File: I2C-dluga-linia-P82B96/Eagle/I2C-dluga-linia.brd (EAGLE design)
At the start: 100 x 80 mm, 7 parts

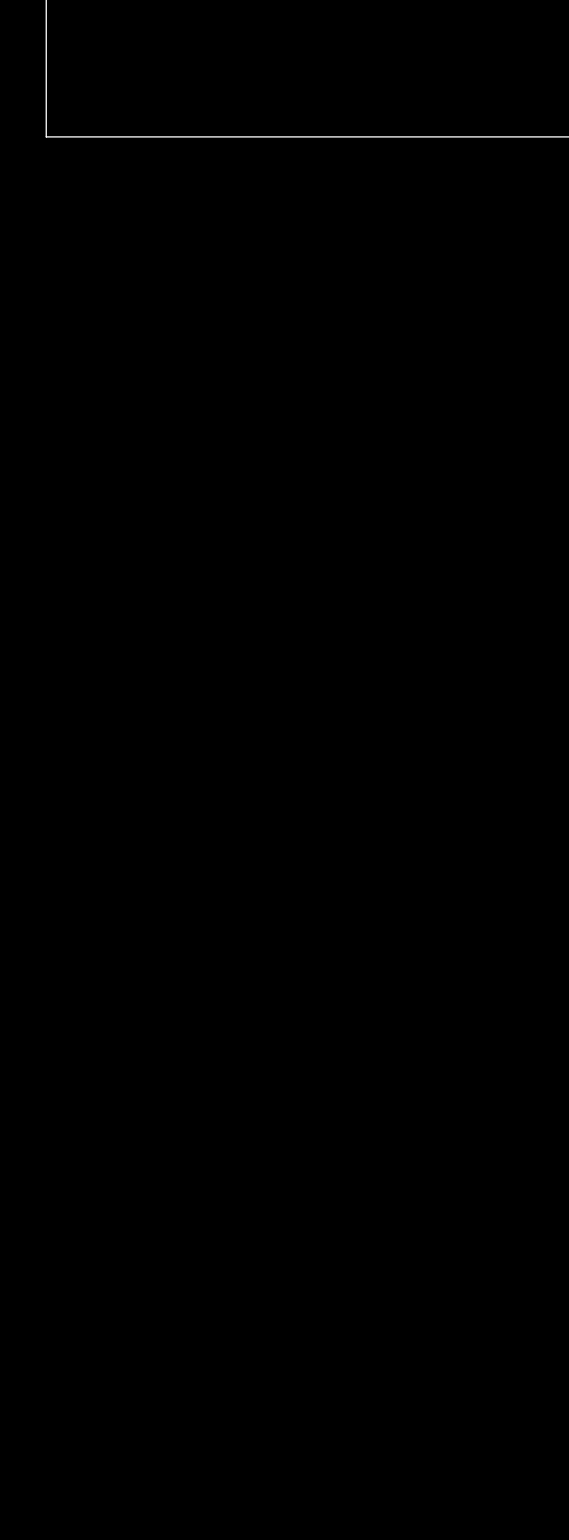
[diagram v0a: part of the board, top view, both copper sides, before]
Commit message: złącza do układów
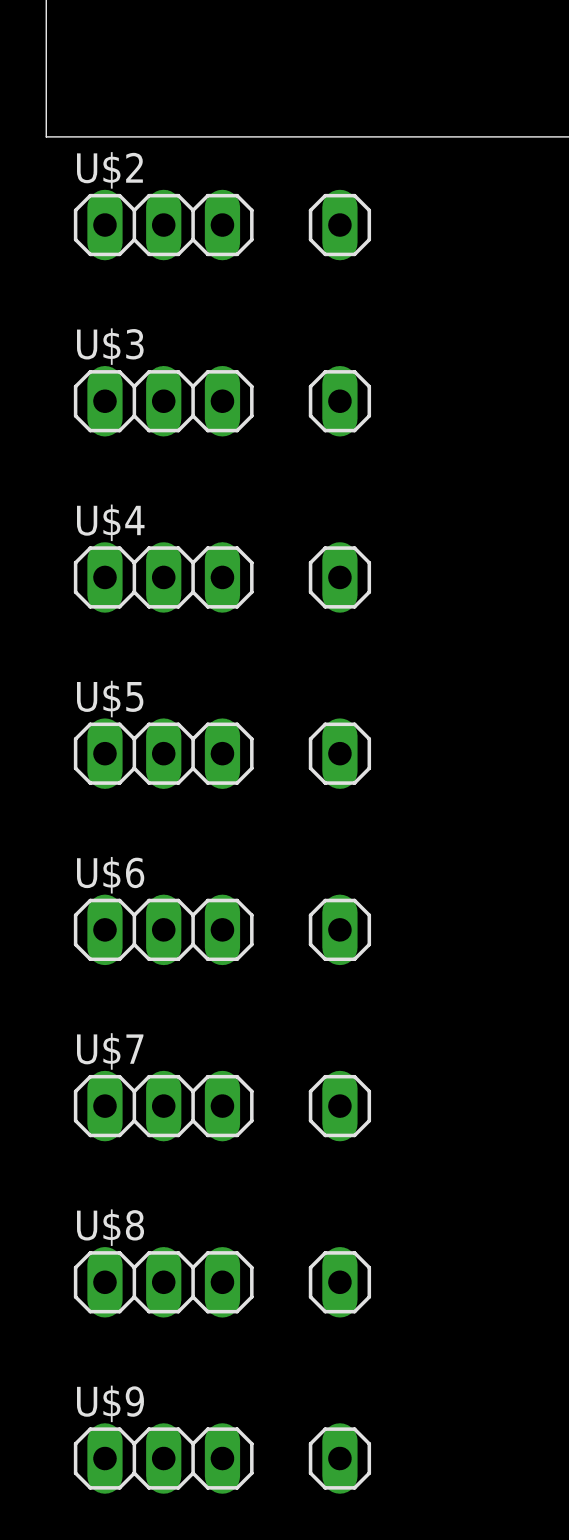
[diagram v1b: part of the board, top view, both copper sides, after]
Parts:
- added U$2, U$3, U$4, U$5, U$6, U$7, U$8, U$9: PINHD5-4, RD:1X5-4
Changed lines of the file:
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@@
 <?xml version="1.0" encoding="utf-8"?>
 <!DOCTYPE eagle SYSTEM "eagle.dtd">
-<eagle version="7.3.0">
+<eagle version="6.4">
 <drawing>
 <settings>
@@
 <pass name="Default">
 <param name="RoutingGrid" value="50mil"/>
-<param name="AutoGrid" value="1"/>
-<param name="Efforts" value="0"/>
-<param name="TopRouterVariant" value="1"/>
 <param name="tpViaShape" value="round"/>
-<param name="PrefDir.1" value="a"/>
+<param name="PrefDir.1" value="|"/>
 <param name="PrefDir.2" value="0"/>
 <param name="PrefDir.3" value="0"/>
@@
 <param name="PrefDir.14" value="0"/>
 <param name="PrefDir.15" value="0"/>
-<param name="PrefDir.16" value="a"/>
+<param name="PrefDir.16" value="-"/>
 <param name="cfVia" value="8"/>
 <param name="cfNonPref" value="5"/>
@@
 <element name="R4" library="resistor" package="R1206" value="2.2k" x="34.29" y="46.99" rot="R90"/>
 <element name="U$1" library="P82B96" package="SOIC8" value="P82B96" x="27.94" y="46.355" rot="R270"/>
+<element name="U$2" library="RD" package="1X5-4" value="PINHD5-4" x="7.62" y="-3.81"/>
+<element name="U$3" library="RD" package="1X5-4" value="PINHD5-4" x="7.62" y="-11.43"/>
+<element name="U$4" library="RD" package="1X5-4" value="PINHD5-4" x="7.62" y="-19.05"/>
+<element name="U$5" library="RD" package="1X5-4" value="PINHD5-4" x="7.62" y="-26.67"/>
+<element name="U$6" library="RD" package="1X5-4" value="PINHD5-4" x="7.62" y="-34.29"/>
+<element name="U$7" library="RD" package="1X5-4" value="PINHD5-4" x="7.62" y="-41.91"/>
+<element name="U$8" library="RD" package="1X5-4" value="PINHD5-4" x="7.62" y="-49.53"/>
+<element name="U$9" library="RD" package="1X5-4" value="PINHD5-4" x="7.62" y="-57.15"/>
 </elements>
 <signals>

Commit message: Podłączone złącza
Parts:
- removed U$2, U$3, U$4, U$5, U$6, U$7, U$8, U$9: PINHD5-4, RD:1X5-4
- added X1, X2: 22-23-2051, con-molex:22-23-2051
- added X3, X4, X5, X6: 22-23-2041, con-molex:22-23-2041
- moved D1 39.9 mm to (6.35, 8.89), flipped to the bottom, turned to 0 degrees
- moved R1 38.7 mm to (7.62, 16.5), flipped to the bottom
- moved R3 37.8 mm to (24.1, 11.4), flipped to the bottom, turned to 180 degrees
- moved D2 34.3 mm to (16.5, 8.89), flipped to the bottom, turned to 180 degrees
- moved U$1 31.0 mm to (19.7, 16.5), flipped to the bottom, turned to 0 degrees
- moved R4 29.9 mm to (27.9, 17.8), flipped to the bottom, turned to 0 degrees
- moved R2 29.2 mm to (17.8, 21.6), flipped to the bottom, turned to 180 degrees
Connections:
- net GND: now also X1.4, X2.4, X3.3, X4.3, X5.3, X6.3
- net L-SCL: now also X1.3, X2.3
- net L-SDA: now also X1.5, X2.5
- net L-VCC: now also X1.2, X2.2
- net SCL: now also X3.2, X4.2, X5.2, X6.2
- net SDA: now also X3.4, X4.4, X5.4, X6.4
- net VCC: now also X1.1, X2.1, X3.1, X4.1, X5.1, X6.1
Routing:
- net VCC: track 2.54 -> 60.5 mm
- net SCL: track 4.19 -> 48.4 mm
- net SDA: track 19.8 -> 51.7 mm
- net L-SDA: track 12.3 -> 24.1 mm
- net L-SCL: track 20.9 -> 28.2 mm
- net L-VCC: track 24.3 -> 30.4 mm
- added copper zone on layer 16, net GND
- removed copper zone on layer 1, net GND
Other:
- board size 100 x 80 mm -> 38.1 x 35.6 mm

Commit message: PCB
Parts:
- added C1, C2: 22p, rcl:C1206
- added C3: (no value), rcl:E5-10,5
- added C4: (no value), rcl:E3,5-8
- moved D2 2.29 mm to (14.6, 7.62)
- moved D1 1.42 mm to (5.71, 7.62)
- moved X1 1.27 mm to (8.89, 20.3)
- moved X2 1.27 mm to (8.89, 11.4)
- moved R3 0.90 mm to (23.5, 10.8)
- moved R1 0.64 mm to (7.62, 15.9)
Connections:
- net GND: now also C1.2, C2.2, C3.-, C4.-, X1.5, X2.5, X3.4, X4.4, X5.4, X6.4; no longer X1.4, X2.4, X3.3, X4.3, X5.3, X6.3
- net L-SDA: now also X1.4, X2.4; no longer X1.5, X2.5
- net L-VCC: now also C3.+
- net SCL: now also C2.1
- net SDA: now also C1.1, X3.3, X4.3, X5.3, X6.3; no longer X3.4, X4.4, X5.4, X6.4
- net VCC: now also C4.+
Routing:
- net SDA: track 51.7 -> 44.8 mm
- net L-SDA: track 24.1 -> 30.7 mm
- net L-VCC: track 30.4 -> 35.7 mm
- net L-SCL: track 28.2 -> 30.3 mm
- net VCC: track 60.5 -> 62.2 mm
- net SCL: track 48.4 -> 49.4 mm

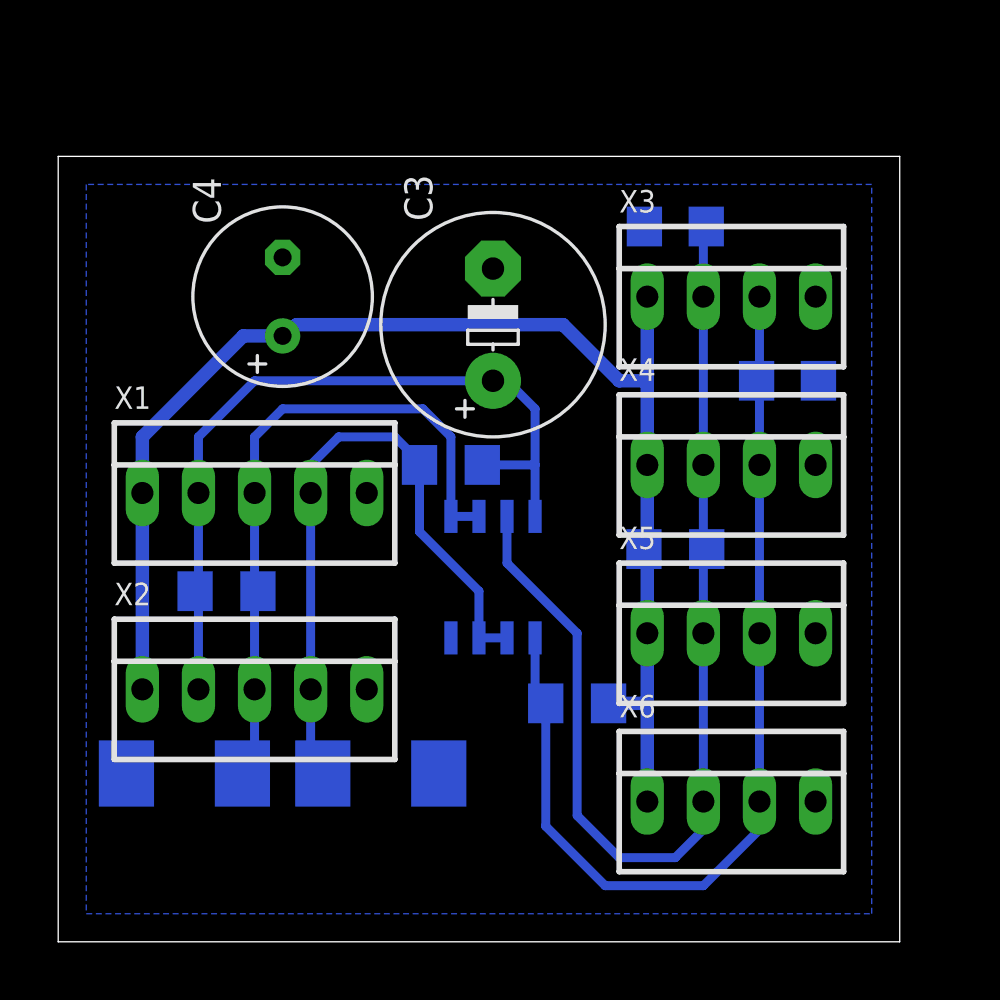
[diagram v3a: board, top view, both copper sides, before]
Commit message: Dodatkowe gniazdo zasilania układów
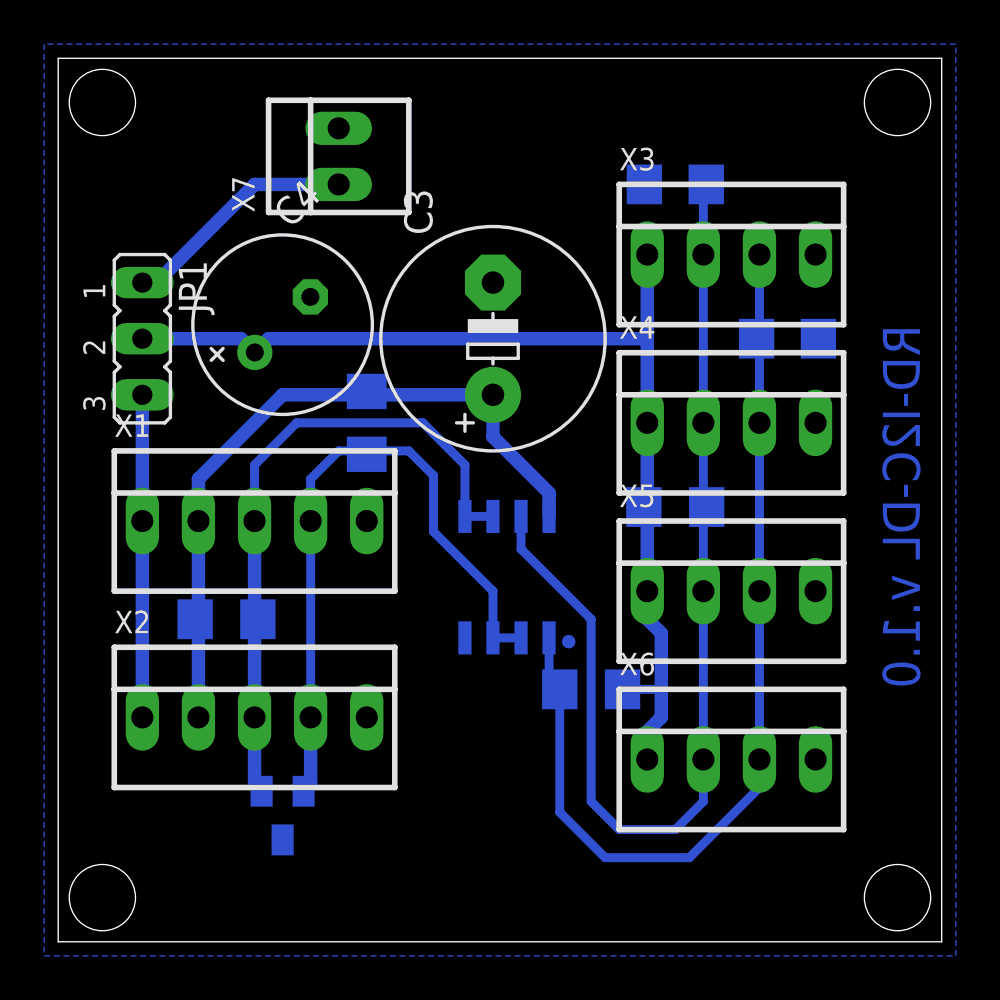
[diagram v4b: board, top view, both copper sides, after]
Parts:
- removed D1, D2: (no value), diode:MELF-MLL41
- added D3: BAT54A, diode:SOT23
- added JP1: (no value), jumper:JP2
- added X7: 22-23-2021, con-molex:22-23-2021
- moved R2 4.26 mm to (14.0, 23.5), turned to 90 degrees
- moved C1 1.91 mm to (33.0, 27.3)
- moved C2 1.91 mm to (27.9, 34.3)
- moved X4 1.91 mm to (30.5, 23.5)
- moved X6 1.91 mm to (30.5, 8.26)
- moved X5 1.90 mm to (30.5, 15.9)
- moved R4 1.90 mm to (27.9, 19.7)
- moved X3 1.90 mm to (30.5, 31.1)
- moved C4 1.27 mm to (10.2, 27.9), turned to 45 degrees
- moved R1 1.27 mm to (7.62, 14.6)
- moved X1 1.27 mm to (8.89, 19.1)
- moved X2 1.27 mm to (8.89, 10.2)
- moved R3 0.90 mm to (24.1, 11.4)
- moved C3 0.64 mm to (19.7, 27.3)
- moved U$1 0.64 mm to (20.3, 16.5)
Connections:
- new net N$1: JP1.3, X1.1, X2.1
- new net N$2: JP1.1, X7.1
- net GND: now also D3.3, X7.2; no longer D1.A, D2.A
- net L-SCL: now also D3.1; no longer D1.C
- net L-SDA: now also D3.2; no longer D2.C
- net VCC: now also JP1.2; no longer X1.1, X2.1
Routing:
- net N$1: track 0.00 -> 14.6 mm
- net VCC: track 62.2 -> 48.7 mm
- net N$2: track 0.00 -> 10.7 mm
- net L-VCC: track 35.7 -> 32.5 mm
- net SDA: track 44.8 -> 43.6 mm
- net SCL: track 49.4 -> 48.5 mm
- net L-SCL: track 30.3 -> 29.7 mm
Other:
- board size 38.1 x 35.6 mm -> 40 x 40 mm
- board text added: "RD-I2C-DL v.1.0"
